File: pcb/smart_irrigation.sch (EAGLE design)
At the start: 31 parts, among them IC1 TMP36, IC2 7805DT, IC3 7833DT, IC4 DS1307, J1 1X2-3.5MM, Q1 IRF730, Q2 32.768, T1 2N3904, U1 BL600

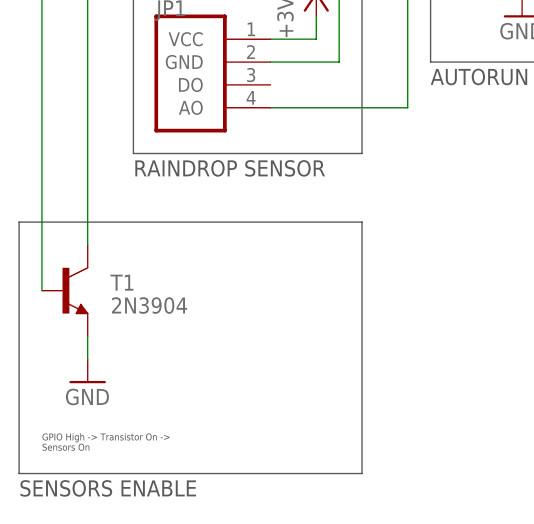
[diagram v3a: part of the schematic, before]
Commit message: PCB: Reposition all sensor headers near edge
Since headers will have cables running off into the sensors themselves
(aside from temp), their respective headers should be at the edges of
the board. The raindrop sensor, however, is a breakout board itself with
its own header, so it has been placed so that its external header is
facing the edge of the board as well.
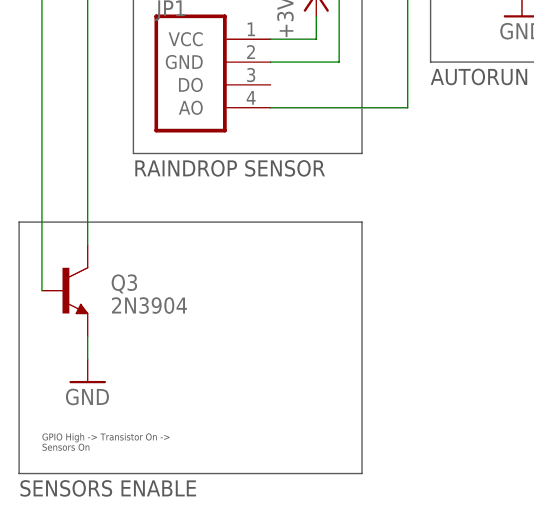
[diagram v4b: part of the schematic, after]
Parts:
- renumbered T1 to Q3
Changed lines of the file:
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@@
 <part name="SUPPLY3" library="supply2" deviceset="+9V" device=""/>
 <part name="GND9" library="supply1" deviceset="GND" device=""/>
-<part name="T1" library="transistor" deviceset="2N3904" device=""/>
+<part name="Q3" library="transistor" deviceset="2N3904" device=""/>
 <part name="GND1" library="supply1" deviceset="GND" device=""/>
 </parts>
@@
 <instance part="SUPPLY3" gate="G$1" x="162.56" y="68.58"/>
 <instance part="GND9" gate="1" x="170.18" y="43.18"/>
-<instance part="T1" gate="G1" x="15.24" y="43.18" smashed="yes">
+<instance part="Q3" gate="G1" x="15.24" y="43.18" smashed="yes">
 <attribute name="NAME" x="20.32" y="43.18" size="1.778" layer="95"/>
 <attribute name="VALUE" x="20.32" y="40.64" size="1.778" layer="96"/>
@@
 </segment>
 <segment>
-<pinref part="T1" gate="G1" pin="E"/>
+<pinref part="Q3" gate="G1" pin="E"/>
 <pinref part="GND1" gate="1" pin="GND"/>
 <wire x1="17.78" y1="38.1" x2="17.78" y2="35.56" width="0.1524" layer="91"/>
@@
 <wire x1="55.88" y1="157.48" x2="12.7" y2="157.48" width="0.1524" layer="91"/>
 <wire x1="12.7" y1="157.48" x2="12.7" y2="43.18" width="0.1524" layer="91"/>
-<pinref part="T1" gate="G1" pin="B"/>
+<pinref part="Q3" gate="G1" pin="B"/>
 <label x="12.7" y="78.74" size="1.778" layer="95" rot="R90"/>
 </segment>
@@
 <pinref part="IC1" gate="A1" pin="GND"/>
 <wire x1="40.64" y1="137.16" x2="40.64" y2="134.62" width="0.1524" layer="91"/>
-<pinref part="T1" gate="G1" pin="C"/>
+<pinref part="Q3" gate="G1" pin="C"/>
 <wire x1="40.64" y1="134.62" x2="17.78" y2="134.62" width="0.1524" layer="91"/>
 <wire x1="17.78" y1="134.62" x2="17.78" y2="104.14" width="0.1524" layer="91"/>
